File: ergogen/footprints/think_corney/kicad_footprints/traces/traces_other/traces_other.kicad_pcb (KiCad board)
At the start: 2 copper layers, 130.3 x 86.5 mm, 112 parts

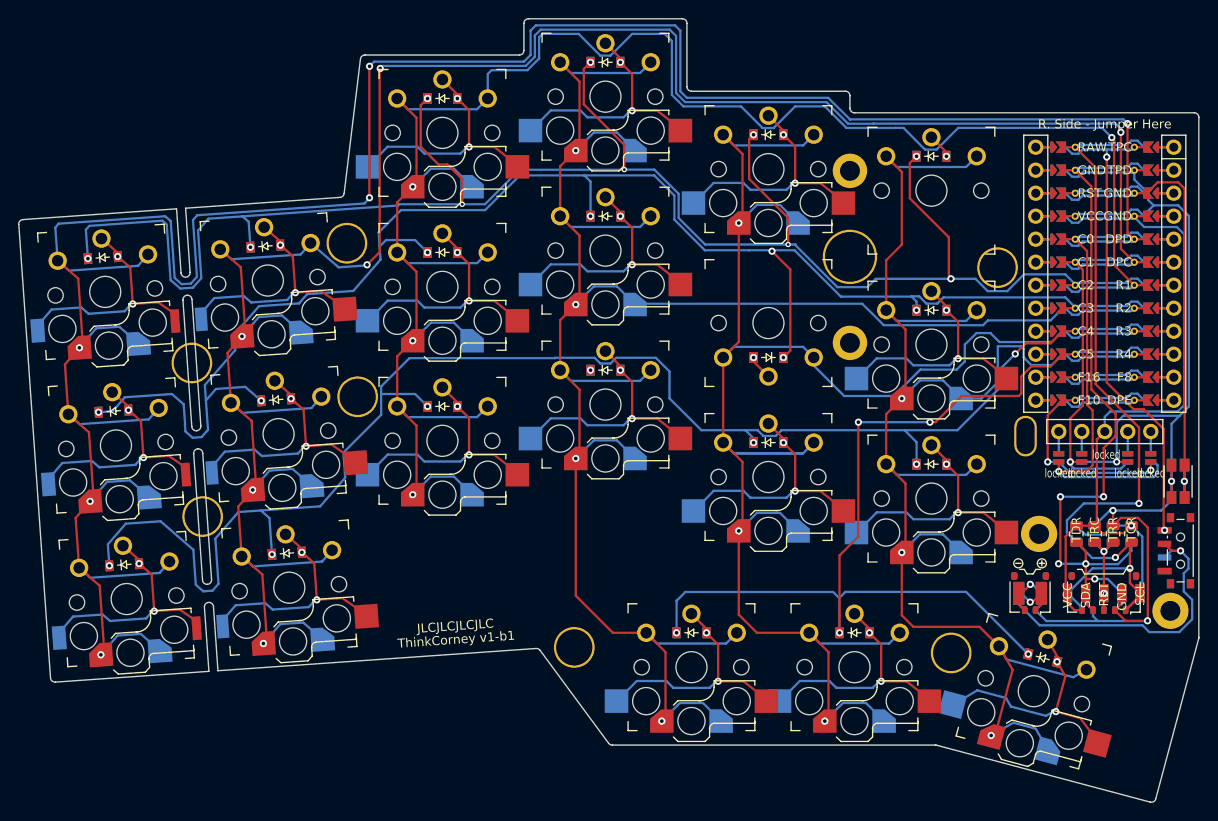
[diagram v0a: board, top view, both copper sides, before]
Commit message: Ergogen: Moved reset switch closer to board edge
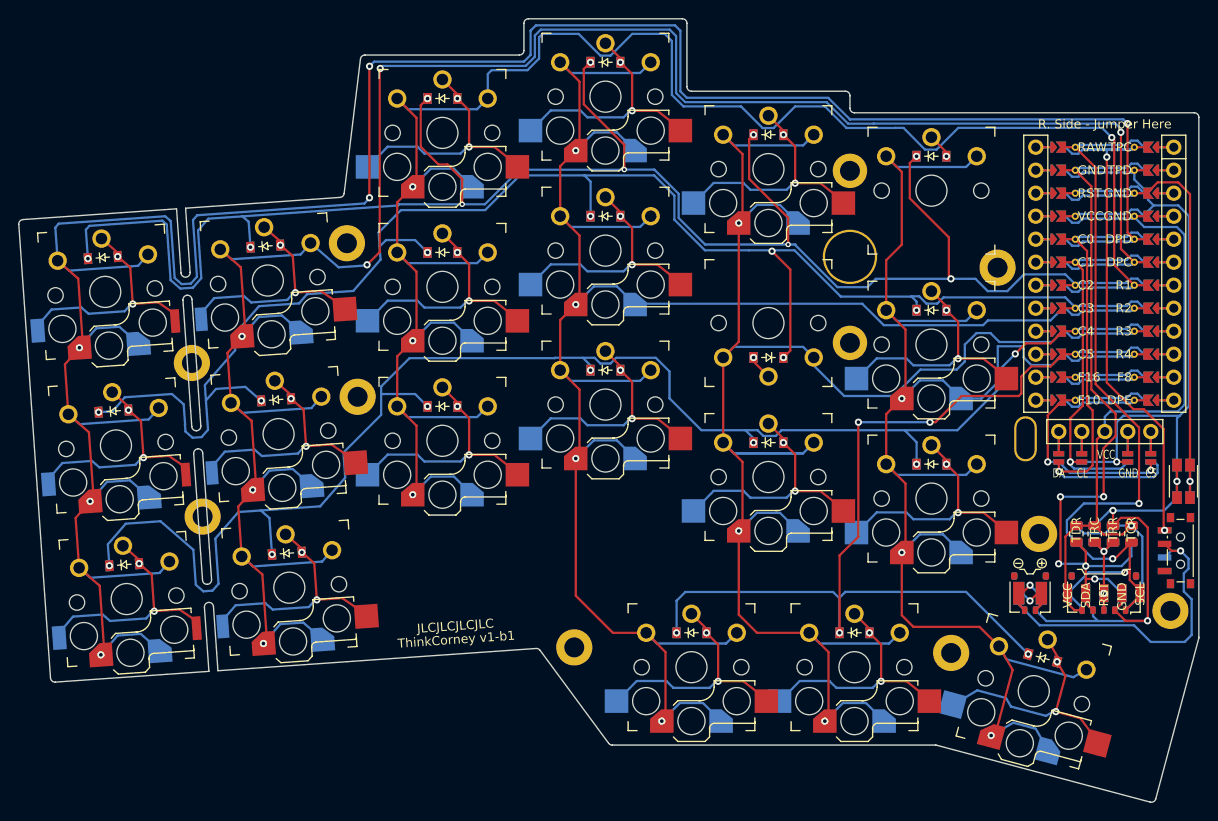
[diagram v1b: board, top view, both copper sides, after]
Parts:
- moved P38" 0.60 mm to (8.69, 24.2)
- moved SW2 0.60 mm to (8.69, 24.2)
- moved H1 0.30 mm to (-8.75, 19.5)
- moved P34" 0.30 mm to (-8.75, 19.5)
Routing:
- net RAW: track 55.4 -> 60.8 mm
- net GND: track 149.8 -> 147.0 mm
- net DISP1_5: track 2.45 -> 4.90 mm
- net DISP1_4: track 2.45 -> 4.90 mm
- net DISP1_2: track 2.45 -> 4.90 mm
- net DISP1_1: track 2.45 -> 4.90 mm
- net BAT_P: track 40.3 -> 38.8 mm
- net R3: track 169.9 -> 171.1 mm
